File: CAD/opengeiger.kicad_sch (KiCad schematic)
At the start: 90 parts, among them J1 Conn_01x04, J10 Conn_01x04, J3 Conn_01x06, J5 Conn_01x04, J8 USB_C_Receptacle_USB2.0, Q1 STN0214, Q2 PMBT2222A,215, Q3 DMG2302UK-7, Q4 UMH3N, SW1 TL3301NF160QG/TR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

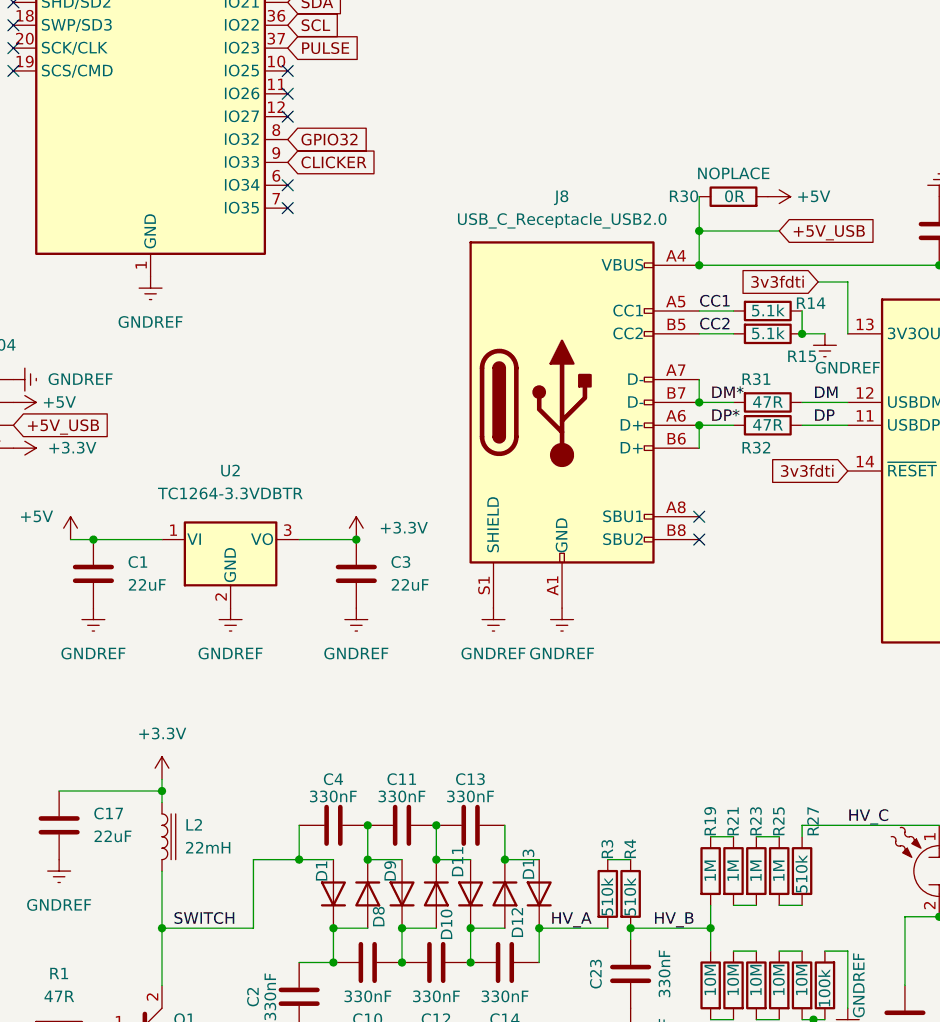
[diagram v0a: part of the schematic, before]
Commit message: Feat: Added LCSC part numbers to schematics
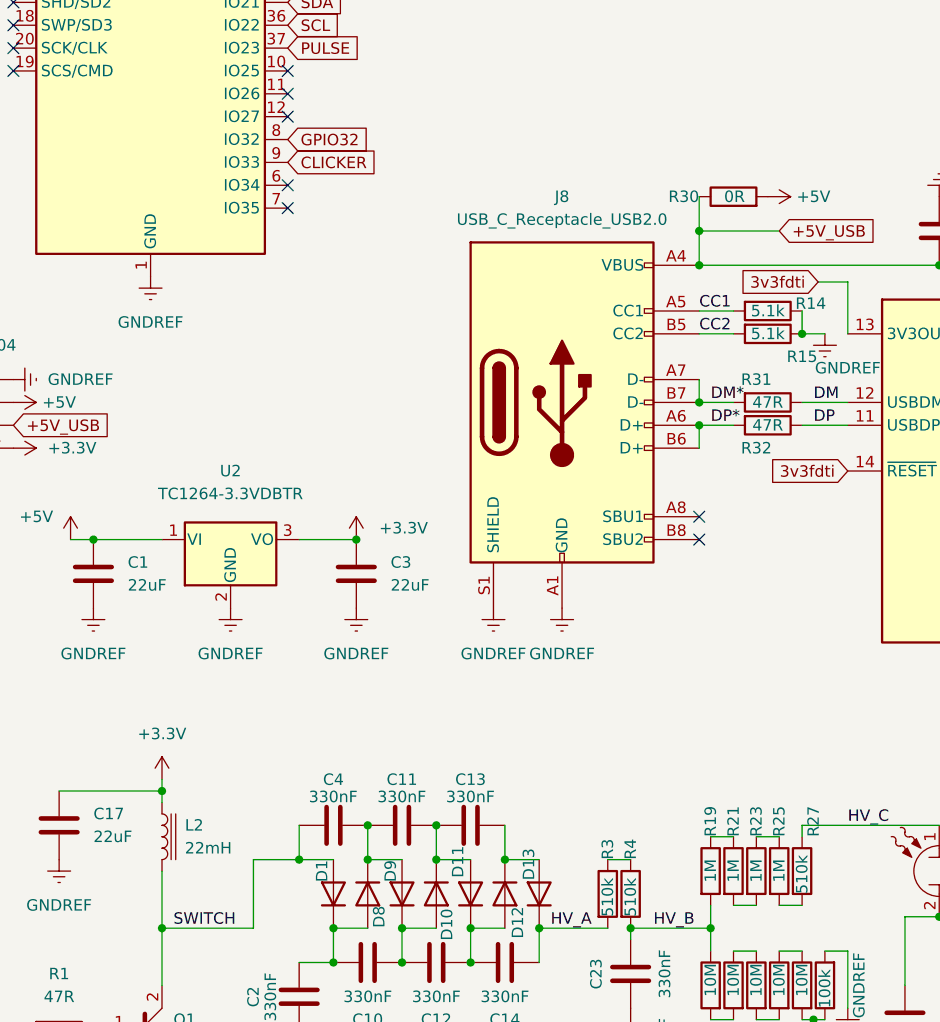
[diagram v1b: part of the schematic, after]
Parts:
- C1, C17, C3, C5: GENERIC (none) -> YES; LCSC Part # (none) -> C398815
- C10, C11, C12, C13, C14, C2, C23, C24, C4: GENERIC (none) -> NO; LCSC Part # (none) -> C710477
- C15, C16, C6, C8, C9: LCSC Part # (none) -> C14663; MPN 06035C104KAT4A -> CC0603KRX7R9BB104; Supplier Part Number 478-10346-1-ND -> 311-1344-2-ND
- C7: LCSC Part # (none) -> C1664; MPN CC0603KRX7R9BB331 -> CL10C331JB8NNNC; Supplier Part Number 311-1186-6-ND -> 1276-1073-2-ND
- D1, D10, D11, D12, D13, D8, D9: LCSC Part # (none) -> C434030
- D14, D2, D3, D4, D5, D6, D7: value 0603RBD0700S01 -> RED_LED; LCSC Part # (none) -> C2286; MPN 0603RBD0700S01 -> LTST-C191KRKT
- J1, J10, J5: LCSC Part # (none) -> C2691448
- J3: LCSC Part # (none) -> C37208
- J8: LCSC Part # (none) -> C2765186
- L2: LCSC Part # (none) -> C1330068
- Q1: LCSC Part # (none) -> C2969811
- Q2: LCSC Part # (none) -> C23869
- Q3: LCSC Part # (none) -> C460977
- Q4: LCSC Part # (none) -> C62892
- R1, R31, R32: LCSC Part # (none) -> C23182
- R10, R11, R12, R13, R33, R34, R9: LCSC Part # (none) -> C22966
- R14, R15: LCSC Part # (none) -> C23186
- R16, R17, R18, R2, R8: LCSC Part # (none) -> C25804
- R19, R21, R23, R25: LCSC Part # (none) -> C253347
- R20, R22, R24, R26, R28: LCSC Part # (none) -> C2075848
- R27, R3, R4: LCSC Part # (none) -> C17990
- R29, R6: LCSC Part # (none) -> C25803
- R30: LCSC Part # (none) -> C17888; PLACE NOPLACE -> (none)
- R5: LCSC Part # (none) -> C22843
- R7: LCSC Part # (none) -> C22967
- SW1, SW2: LCSC Part # (none) -> C255812
- U1: LCSC Part # (none) -> C701343
- U2: LCSC Part # (none) -> C6186
- U3: LCSC Part # (none) -> C132160

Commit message: Feat: Update to 0.2.2
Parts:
- added F1, F2: 6.35mm Fuse holder, eikgeiger:FC-102-22, symbol Connector:TestPoint_Small
- G1: MPN (none) -> SBM-20
- Q4: MPN (none) -> UMH3N; Supplier Part Number (none) -> UMH3NFHATNCT-ND
- U3: MPN (none) -> FT231XS; Supplier Part Number (none) -> 768-1129-1-ND
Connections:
- no-connect marks 28 -> 30
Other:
- note added: "Fuse holder placeholders to get them in bom"
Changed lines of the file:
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@@
     (title "Main Schematic")
     (date "2022-11-03")
-    (rev "V.0.2.1")
+    (rev "V.0.2.2")
     (company "EIK IDEVERKSTED OPENGEIGER")
   )
@@
   (no_connect (at 130.81 22.86))
   (no_connect (at 53.34 83.82))
+  (no_connect (at 257.81 41.91))
   (no_connect (at 270.51 31.75))
   (no_connect (at 257.81 22.86))
   (no_connect (at 53.34 68.58))
+  (no_connect (at 257.81 46.99))
   (no_connect (at 53.34 58.42))
   (no_connect (at 53.34 55.88))
@@
     (stroke (width 0) (type default))
   )
+  (text "Fuse holder placeholders \nto get them in bom" (at 256.54 54.61 0)
+    (effects (font (size 1.27 1.27)) (justify left bottom))
+  )
   (label "CBUS1" (at 153.67 123.19 0) (fields_autoplaced)
     (effects (font (size 1.27 1.27)) (justify left bottom))
@@
       (effects (font (size 1.27 1.27)) hide)
     )
+    (property "MPN" "UMH3N" (at 184.15 97.79 0)
+      (effects (font (size 1.27 1.27)) hide)
+    )
+    (property "Supplier Part Number" "UMH3NFHATNCT-ND" (at 184.15 97.79 0)
+      (effects (font (size 1.27 1.27)) hide)
+    )
     (pin "1")
     (pin "2")
@@
       (effects (font (size 1.27 1.27)) hide)
     )
+    (property "MPN" "SBM-20" (at 125.73 157.48 0)
+      (effects (font (size 1.27 1.27)) hide)
+    )
+    (property "Supplier Part Number" "" (at 125.73 157.48 0)
+      (effects (font (size 1.27 1.27)) hide)
+    )
     (pin "1")
     (pin "2")
@@
     )
   )
+  (symbol (lib_id "Connector:TestPoint_Small") (at 257.81 46.99 0) (unit 1)
+    (in_bom yes) (on_board yes) (dnp no) (fields_autoplaced)
+    (property "Reference" "F2" (at 259.08 45.72 0)
+      (effects (font (size 1.27 1.27)) (justify left))
+    )
+    (property "Value" "6.35mm Fuse holder" (at 259.08 48.26 0)
+      (effects (font (size 1.27 1.27)) (justify left))
+    )
+    (property "Footprint" "eikgeiger:FC-102-22" (at 262.89 46.99 0)
+      (effects (font (size 1.27 1.27)) hide)
+    )
+    (property "Datasheet" "~" (at 262.89 46.99 0)
+      (effects (font (size 1.27 1.27)) hide)
+    )
+    (property "LCSC Part #" "C3206833" (at 257.81 46.99 0)
+      (effects (font (size 1.27 1.27)) hide)
+    )
+    (property "MPN" "FC-102  BRIGHT TIN" (at 257.81 46.99 0)
+      (effects (font (size 1.27 1.27)) hide)
+    )
+    (property "Supplier Part Number" "507-FC-102BRIGHTTIN-ND" (at 257.81 46.99 0)
+      (effects (font (size 1.27 1.27)) hide)
+    )
+    (pin "1")
+    (instances
+      (project "opengeiger"
+        (path "/8a0213a9-e710-4867-a1ff-72258b44c96e"
+          (reference "F2") (unit 1)
+        )
+      )
+    )
+  )
   (symbol (lib_id "power:+3.3V") (at 60.96 120.65 0) (unit 1)
     (in_bom yes) (on_board yes) (dnp no) (fields_autoplaced)
@@
       (effects (font (size 1.27 1.27)) hide)
     )
+    (property "MPN" "FT231XS" (at 133.35 113.03 0)
+      (effects (font (size 1.27 1.27)) hide)
+    )
+    (property "Supplier Part Number" "768-1129-1-ND" (at 133.35 113.03 0)
+      (effects (font (size 1.27 1.27)) hide)
+    )
     (pin "1")
     (pin "10")
@@
     )
   )
+  (symbol (lib_id "Connector:TestPoint_Small") (at 257.81 41.91 0) (unit 1)
+    (in_bom yes) (on_board yes) (dnp no) (fields_autoplaced)
+    (property "Reference" "F1" (at 259.08 40.64 0)
+      (effects (font (size 1.27 1.27)) (justify left))
+    )
+    (property "Value" "6.35mm Fuse holder" (at 259.08 43.18 0)
+      (effects (font (size 1.27 1.27)) (justify left))
+    )
+    (property "Footprint" "eikgeiger:FC-102-22" (at 262.89 41.91 0)
+      (effects (font (size 1.27 1.27)) hide)
+    )
+    (property "Datasheet" "~" (at 262.89 41.91 0)
+      (effects (font (size 1.27 1.27)) hide)
+    )
+    (property "LCSC Part #" "C3206833" (at 257.81 41.91 0)
+      (effects (font (size 1.27 1.27)) hide)
+    )
+    (property "MPN" "FC-102  BRIGHT TIN" (at 257.81 41.91 0)
+      (effects (font (size 1.27 1.27)) hide)
+    )
+    (property "Supplier Part Number" "507-FC-102BRIGHTTIN-ND" (at 257.81 41.91 0)
+      (effects (font (size 1.27 1.27)) hide)
+    )
+    (pin "1")
+    (instances
+      (project "opengeiger"
+        (path "/8a0213a9-e710-4867-a1ff-72258b44c96e"
+          (reference "F1") (unit 1)
+        )
+      )
+    )
+  )
   (symbol (lib_id "power:+3.3V") (at 213.36 38.1 0) (unit 1)
     (in_bom yes) (on_board yes) (dnp no)
@@
       (effects (font (size 1.27 1.27)) hide)
     )
+    (property "MPN" "UMH3N" (at 173.99 102.87 0)
+      (effects (font (size 1.27 1.27)) hide)
+    )
+    (property "Supplier Part Number" "UMH3NFHATNCT-ND" (at 173.99 102.87 0)
+      (effects (font (size 1.27 1.27)) hide)
+    )
